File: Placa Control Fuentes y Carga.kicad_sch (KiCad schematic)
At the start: 135 parts, among them J1 TBP01R1-508-02BE, J10 TBP01R1-508-03BE, J2 TBP01R1-508-02BE, J3 TBP01R1-508-02BE, J4 TBP01R1-508-02BE, J5 TBP01R1-508-02BE, J6 TBP01R1-508-02BE, J7 TBP01R1-508-02BE, J8 TBP01R1-508-02BE, J9 TBP01R1-508-02BE, Q1 IRF9540N, Q2 2N3904, Q3 BC558, Q4 BC558, Q5 IRF5305, Q6 BC337, Q7 BC327, U1 ACS724LLCTR-05AB-T, U2 Relay_Module_WB-083, U3 4N35, U4 LM2596S_Modulo_Regulable, U5 Arduino_Nano_ATmega328P, U6 ACS724LLCTR-05AB-T, U7 MAX485E, U8 MAX22445FAWE+, U9 RI3-0505S

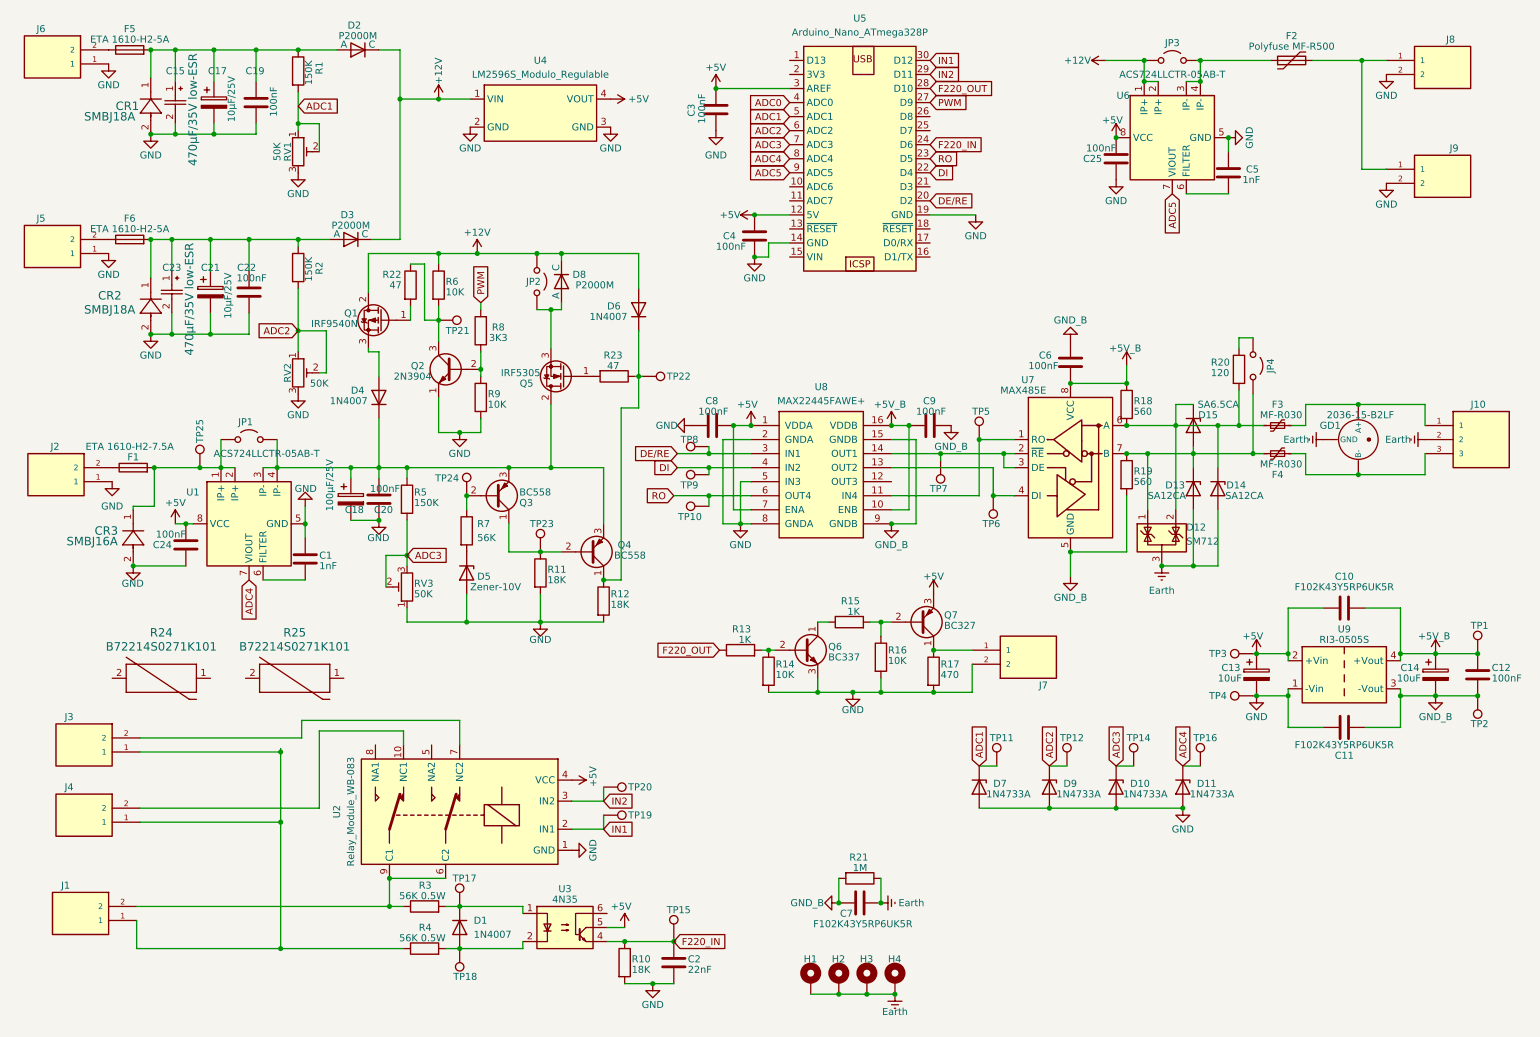
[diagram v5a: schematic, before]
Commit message: feat(pcb): placement inicial y netlist vinculada en placa 2 capas
- Placa 2 capas FR4 1.6 mm; contorno Edge.Cuts ~160 x 95 mm
- 142 footprints colocados (cara top); netlist asociada a pads
- Dominios de tierra en netlist: GND (principal) y GND_B (RS-485 aislado)
- Secciones ubicadas: entrada/OR-ing, LM2596, sensado ACS724, rele,
  RS-485 (MAX485E/MAX22445/RI3-0505S) y deteccion 220 VCA (4N35/GDT)

Pendiente (no incluido en este commit):
- Ruteo de senal y potencia
- Planos/zonas GND y GND_B (validar que NO se unan en cobre)
- Vias de costura y de retorno
- Barrera de fresado bajo U3 (4N35) para creepage 220 VCA
- Anchos de pista de potencia por IPC-2152
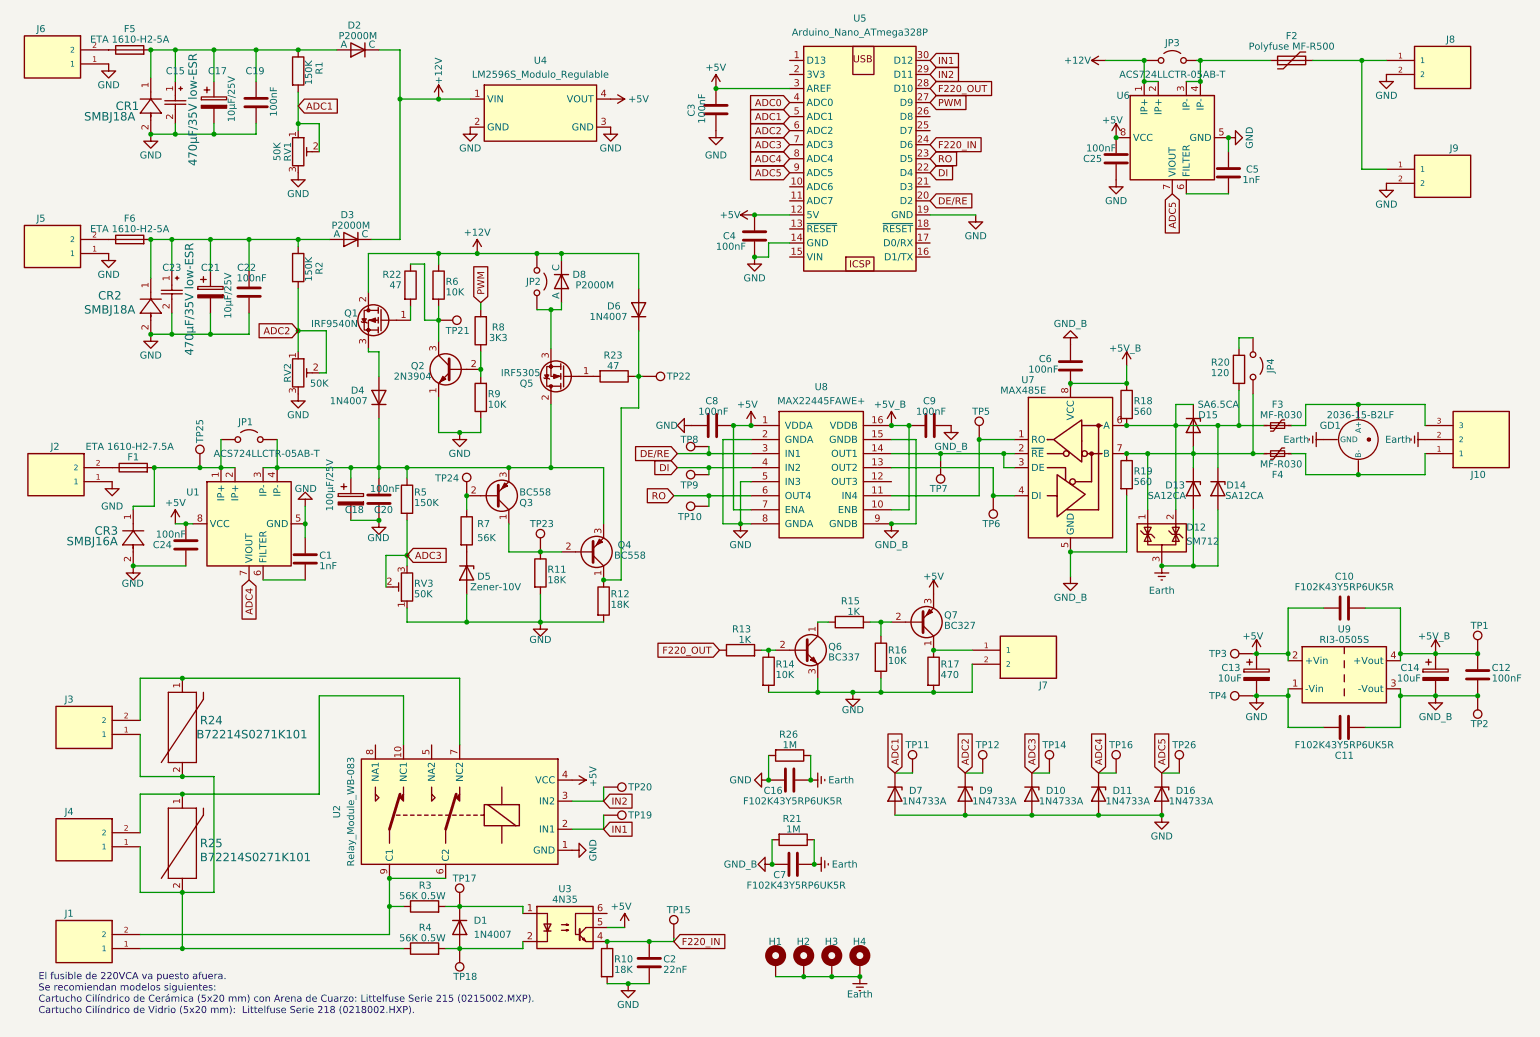
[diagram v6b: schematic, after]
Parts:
- added C16: F102K43Y5RP6UK5R, Damian_PCB:CAP_F_11X5P_VIS, symbol Simbolos1:Cap_Y
- added D16: 1N4733A, Diode_THT:D_DO-41_SOD81_P10.16mm_Horizontal, symbol Diode:1N47xxA
- added R26: 1M, Resistor_THT:R_Axial_DIN0207_L6.3mm_D2.5mm_P7.62mm_Horizontal, symbol Device:R
- added TP26: TestPoint, TestPoint:TestPoint_THTPad_D2.5mm_Drill1.2mm, symbol Connector:TestPoint
- R24, R25: footprint VARS_B72214S0271K101_TDK -> Damian_PCB:VARS_B72214S0271K101_TDK
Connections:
- net +12V: now also D2.1 (C), D3.1 (C), D8.1 (C); no longer D2.2 (C), D3.2 (C), D8.2 (C)
- net ADC5: now also D16.1 (K), TP26.1
- net Earth: now also C16.2, R26.1
- net GND: now also C16.1, D16.2 (A), R26.2
- net at C15.1, C17.1, C19.1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: now also D2.2 (A); no longer D2.1 (A)
- net at C21.1, C22.2, C23.1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: now also D3.2 (A); no longer D3.1 (A)
- net at J4.2, U2.10 (NC1): now also R25.1
- net at J3.2, U2.7 (NC2): now also R24.1
- net at J1.1, J3.1, J4.1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: now also R24.2, R25.2
- net at F3.2, GD1.1 (A+): now also J10.3; no longer J10.1
- net at F4.2, GD1.3 (B-): now also J10.1; no longer J10.3
- net at JP2.2 (B), Q5.3 (S): now also D8.2 (A); no longer D8.1 (A)
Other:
- note added: "El fusible de 220VCA va puesto afuera. Se recomiendan modelos siguientes: Cartucho Cilíndrico de Cerámica (5x20 mm) con Arena de Cuarzo: Littelfuse Serie 215 (0215002.MXP). Cartucho Cilíndrico de Vidrio (5x20 mm): Littelfuse Serie 218 (0218002.HXP)."
- moved on the sheet: C2, C6, C7, D10, D11, D7, D9, H1, H2, H3, H4, J1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

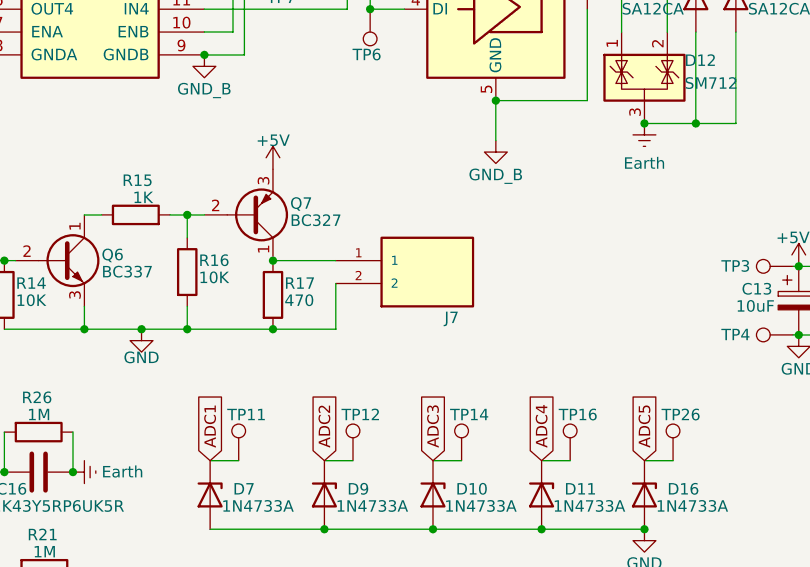
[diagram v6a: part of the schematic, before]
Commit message: feat(pcb): ruteo casi completo + planos GND/+5V/+12V y earth ancho
== Avances mas notables ==
- Ruteo: 682 segmentos (242 F.Cu / 440 B.Cu) + 19 vias
- 57/76 nets ruteadas; solo faltan 2 senales reales: ADC0 y PWM
  (el resto de "unconnected" son pads NC de U5/U2/U3/U8)
- Planos rellenados (locked): GND x4 (masa1-4, F.Cu+B.Cu),
  +5V (cincoV1, F.Cu) y +12V (B.Cu)
- Dominio aislado RS-485 cableado: GND_B (36 seg) y +5V_B (25 seg)
- Earth de proteccion ruteado ancho (3-5 mm, 22 seg)
- 9 keepouts de aislamiento en F.Cu
- Anchos de potencia generosos (+12V/GND/Earth hasta 3-4 mm)

== Pendiente para finalizar ==
- Rutear ADC0 y PWM; dejar ratsnest en cero
- GND_B/+5V_B estan solo como pistas: definir isla/retorno de GND_B
  (hoy NO existe zona de cobre para el retorno aislado)
- Verificar separacion GND vs GND_B (sin cruces ni acoplamiento)
- Reforzar via stitching en los planos GND (solo 19 vias)
- Barrera 220 VCA: confirmar ranura de fresado bajo U3 (4N35) y fijar
  creepage/clearance (faltan: clase de aislamiento, recubrimiento,
  grado de polucion)
- Validar anchos vs IPC-2152 con corrientes reales
- Confirmar stackup/peso de cobre (1 oz?), DRC limpio y serigrafia.
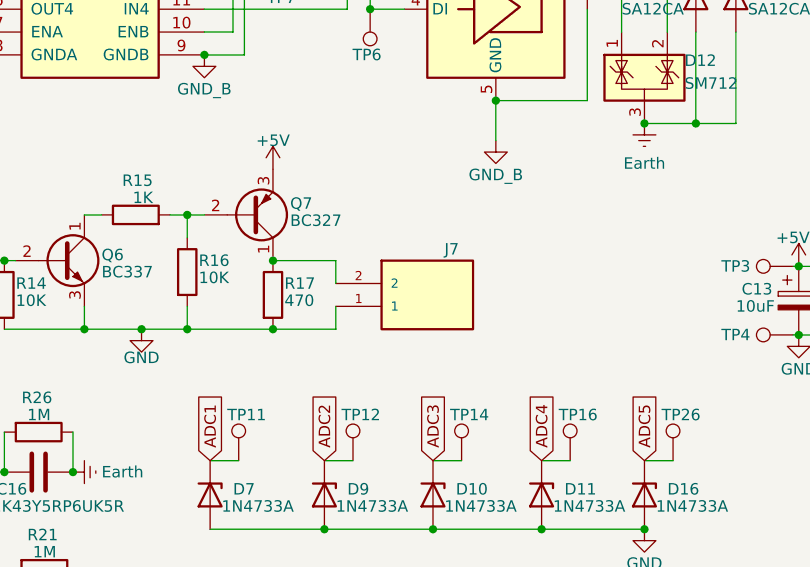
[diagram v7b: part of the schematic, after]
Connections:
- net GND: now also J7.1; no longer J7.2
- net at Q7.1 (C), R17.1: now also J7.2; no longer J7.1
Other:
- moved on the sheet: J7
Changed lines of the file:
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@@
 	(wire
 		(pts
+			(xy 184.785 135.255) (xy 184.785 137.795)
+		)
+		(stroke
+			(width 0)
+			(type default)
+		)
+	)
+	(wire
+		(pts
 			(xy 81.28 55.88) (xy 76.2 55.88)
 		)
@@
 	(wire
 		(pts
-			(xy 184.785 132.715) (xy 184.785 137.795)
-		)
-		(stroke
-			(width 0)
-			(type default)
-		)
-	)
-	(wire
-		(pts
 			(xy 173.355 104.775) (xy 173.355 89.535)
 		)
@@
 	(wire
 		(pts
+			(xy 184.785 130.175) (xy 184.785 132.715)
+		)
+		(stroke
+			(width 0)
+			(type default)
+		)
+	)
+	(wire
+		(pts
 			(xy 241.935 132.08) (xy 241.935 130.81)
 		)
@@
 		(lib_id "TBP01R1-508-02BE:TBP01R1-508-02BE")
 		(at 194.945 132.715 0)
+		(mirror x)
 		(unit 1)
 		(body_style 1)
@@
 		(dnp no)
 		(property "Reference" "J7"
-			(at 196.85 136.525 0)
+			(at 196.85 128.905 0)
 			(show_name no)
 			(do_not_autoplace no)
@@
 		)
 		(property "Value" "TBP01R1-508-02BE"
-			(at 185.293 136.652 0)
+			(at 185.293 128.778 0)
 			(hide yes)
 			(show_name no)

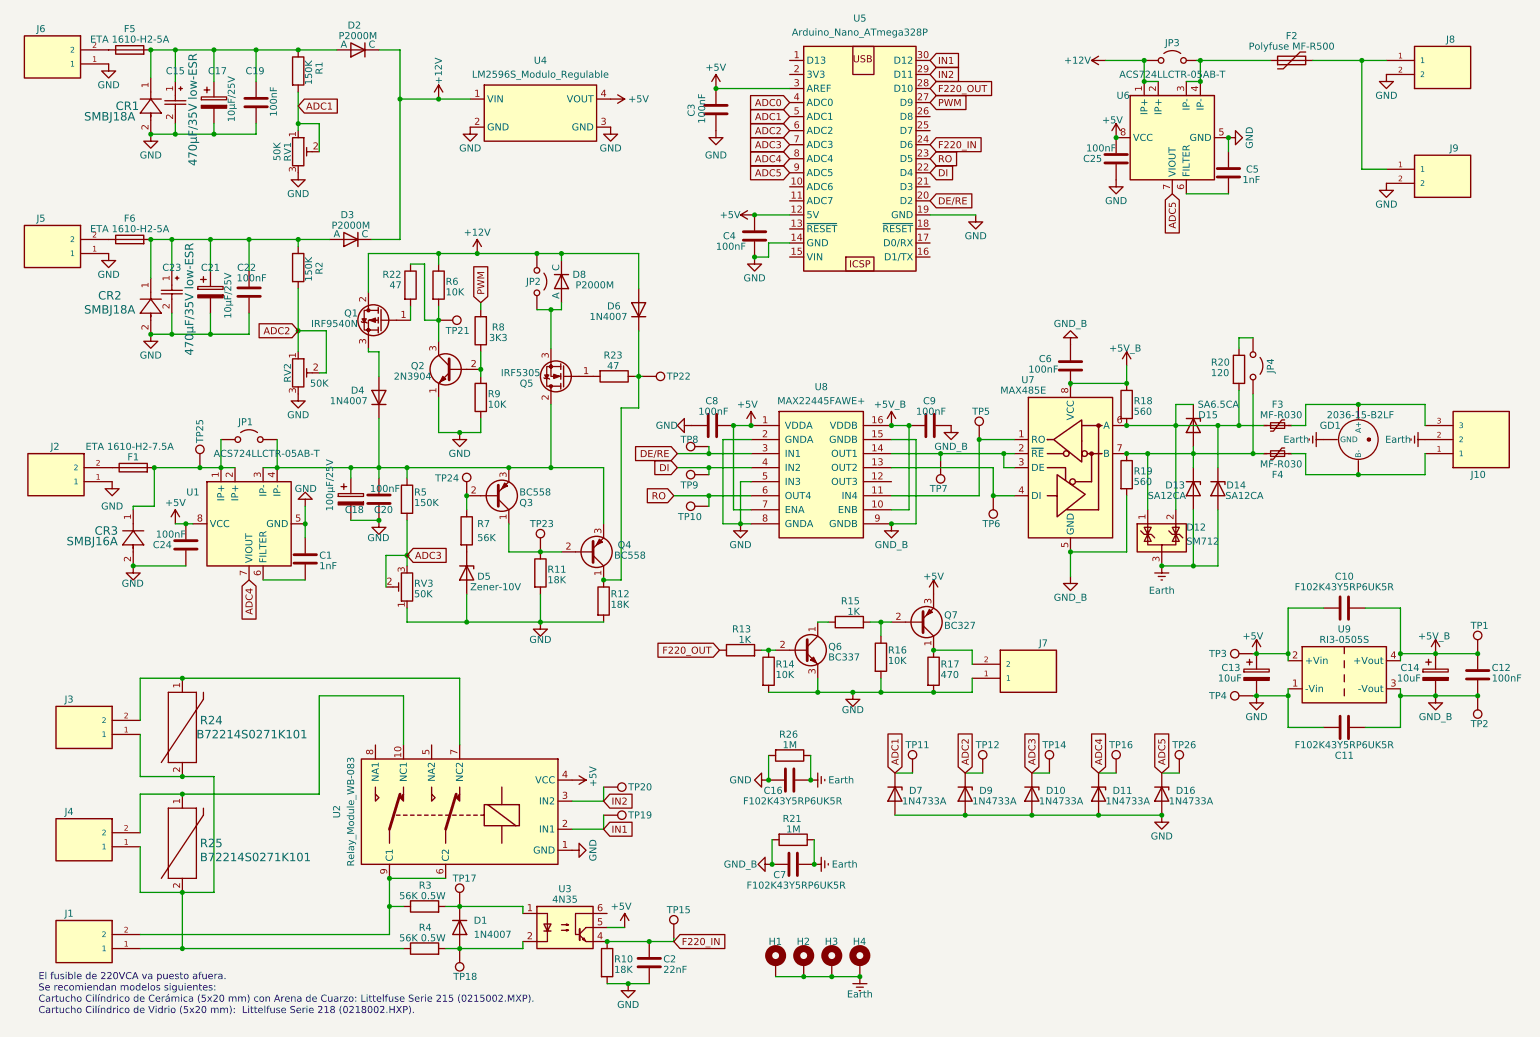
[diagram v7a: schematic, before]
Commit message: wip(pcb): ruteo 58/76 (falta ADC0); GND_B sin plano; barrera 220VCA e IPC pendientes.
feat(pcb): ruteo casi cerrado (solo falta ADC0) + refuerzo de vias

== Avances mas notables ==
- Ruteo: 858 segmentos (340 F.Cu / 518 B.Cu) + 33 vias (+14 vs commit previo)
- 58/76 nets ruteadas; PWM ya ruteado -> unica senal real pendiente: ADC0
- GND densificado (182 seg); +5V (87 seg) completado
- Dominio aislado RS-485 cableado: GND_B (45 seg) y +5V_B (29 seg)
- Earth de proteccion ancho (3-5 mm, 22 seg)
- Planos rellenados (locked): GND x4 (masa1-4, F.Cu+B.Cu), +5V (F.Cu), +12V (B.Cu)
- 9 keepouts de aislamiento en F.Cu

== Pendiente para finalizar ==
- Rutear ADC0; dejar ratsnest en cero
- GND_B/+5V_B siguen solo como pistas: definir isla/retorno vertido de
  GND_B (hoy NO existe zona de cobre para el retorno aislado)
- Verificar separacion GND vs GND_B (sin cruces ni acoplamiento)
- Seguir reforzando via stitching en planos GND (33 vias)
- Barrera 220 VCA: confirmar ranura de fresado bajo U3 (4N35) y fijar
  creepage/clearance (faltan: clase de aislamiento, recubrimiento, polucion)
- Validar anchos vs IPC-2152 con corrientes reales
- Confirmar stackup/peso de cobre (1 oz?), DRC limpio y serigrafia.
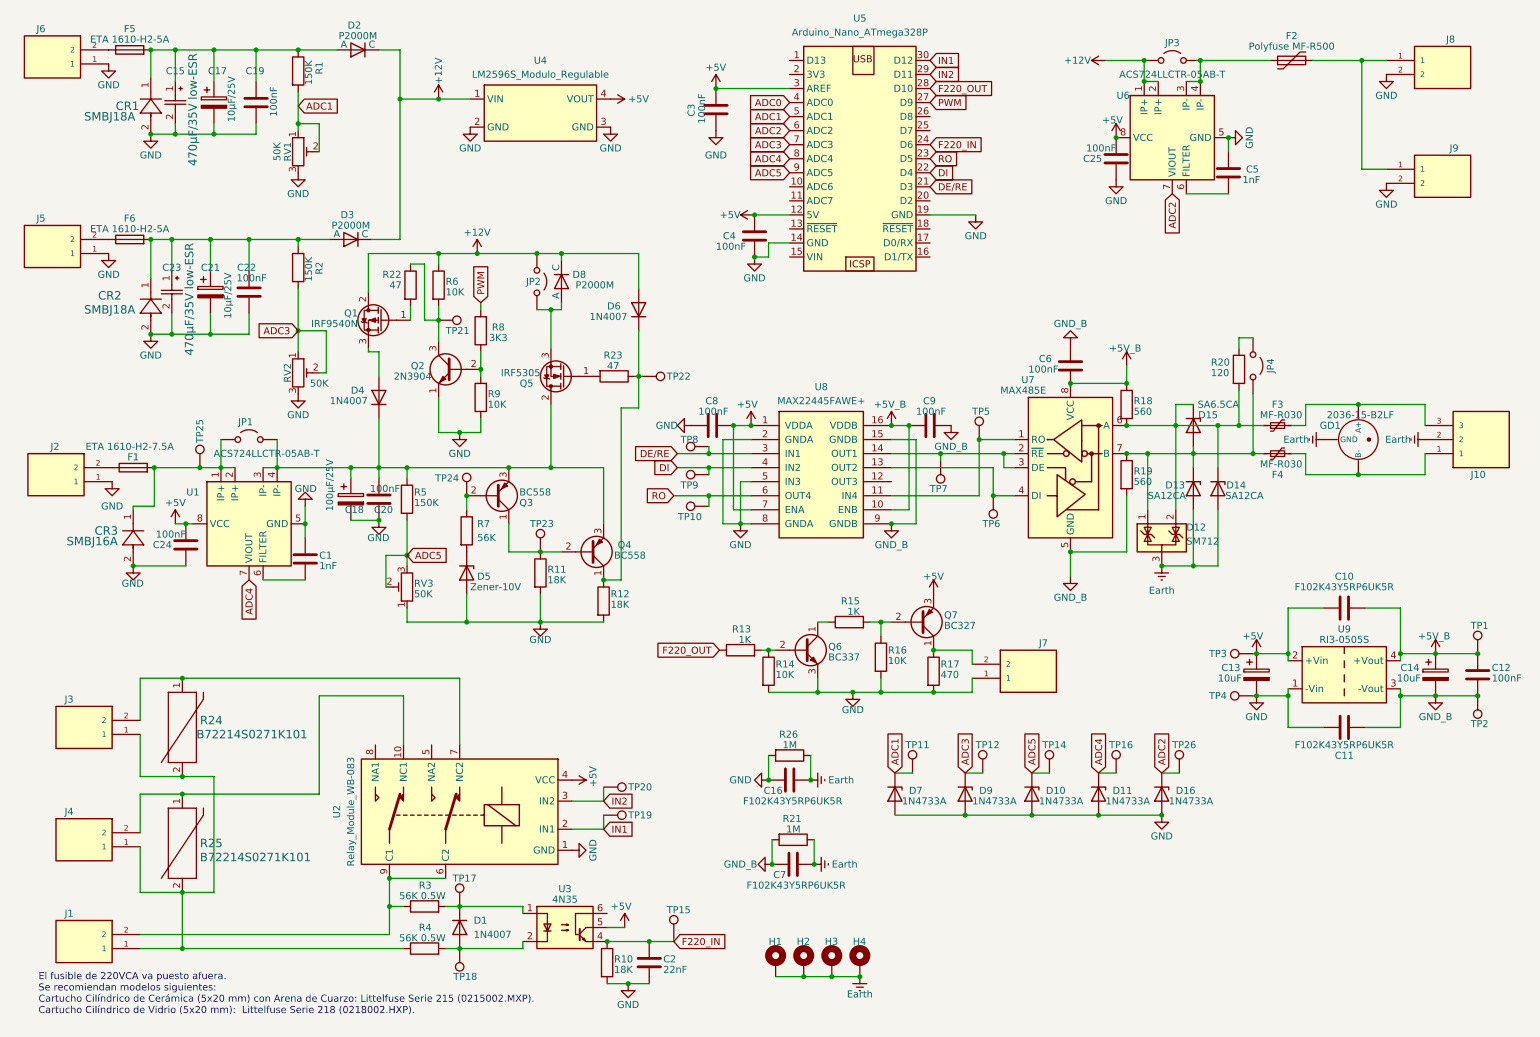
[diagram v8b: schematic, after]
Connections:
- net ADC2: now also D16.1 (K), TP26.1, U6.7 (VIOUT); no longer D9.1 (K), R2.2, RV2.1, RV2.2, TP12.1
- net ADC3: now also D9.1 (K), R2.2, RV2.1, RV2.2, TP12.1; no longer D10.1 (K), R5.2, RV3.2, RV3.3, TP14.1
- net ADC5: now also D10.1 (K), R5.2, RV3.2, RV3.3, TP14.1; no longer D16.1 (K), TP26.1, U6.7 (VIOUT)
- net DE/RE: now also U5.21 (D3); no longer U5.20 (D2)
